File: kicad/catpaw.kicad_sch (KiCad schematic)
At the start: 42 parts, among them J1 Conn_01x01_Socket_red, J2 Conn_01x01_Socket_black, J3 m12,Acode,5pin,femalesocket (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, J4 m8, 4Pin Supply Connector FEM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, J5 m8, 4Pin Supply Connector Bec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, J6 m12,Acode,5pin,femalesocket B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, J7 m12,Acode,5pin,femalesocket C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, J8 Conn_01x01_Pin, SW1 1MD1T1B1M6QES, U1 INA826, U2 LM1458mx

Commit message: Begin Rev1.1
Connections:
- net GND: now also R13.2
- net m8 GNDp: no longer R13.2
- no-connect marks 5 -> 6
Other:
- note added: "(-7.6V)"
- note added: "09/14/26 as per datasheet, (section: ) omit Rg for a gain of 1"
- note added: "09/14/26 simulated via circuitLab omit rakout- connection to input"
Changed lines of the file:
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@@
 		)
 	)
+	(text "09/14/26\nsimulated via circuitLab\nomit rakout- connection to input"
+		(exclude_from_sim no)
+		(at 241.808 125.984 0)
+		(effects
+			(font
+				(size 1.27 1.27)
+			)
+		)
+	)
 	(text "m8 Up+- & m12 Up+- \nare connected in beckhoff"
 		(exclude_from_sim no)
@@
 		)
 	)
+	(text "09/14/26\nas per datasheet, (section:  ) \nomit Rg for a gain of 1"
+		(exclude_from_sim no)
+		(at 86.868 184.15 0)
+		(effects
+			(font
+				(size 1.27 1.27)
+			)
+			(justify left)
+		)
+	)
+	(text "(-7.6V)"
+		(exclude_from_sim no)
+		(at 256.286 116.586 0)
+		(effects
+			(font
+				(size 1.27 1.27)
+			)
+		)
+	)
 	(text "thruhole LED\npanelmount"
 		(exclude_from_sim no)
@@
 	)
 	(no_connect
+		(at 203.2 120.65)
+	)
+	(no_connect
 		(at 63.5 110.49)
 	)
@@
 	(wire
 		(pts
-			(xy 203.2 120.65) (xy 222.25 120.65)
-		)
-		(stroke
-			(width 0)
-			(type default)
-		)
-	)
-	(wire
-		(pts
 			(xy 191.77 149.86) (xy 208.28 149.86)
 		)
@@
 				)
 			)
+		)
+	)
+	(symbol
+		(lib_id "power:GND")
+		(at 222.25 120.65 0)
+		(unit 1)
+		(exclude_from_sim no)
+		(in_bom yes)
+		(on_board yes)
+		(dnp no)
+		(property "Reference" "#PWR06"
+			(at 222.25 127 0)
+			(effects
+				(font
+					(size 1.27 1.27)
+				)
+				(hide yes)
+			)
+		)
+		(property "Value" "GND"
+			(at 222.25 124.714 0)
+			(effects
+				(font
+					(size 1.27 1.27)
+				)
+			)
+		)
+		(property "Footprint" ""
+			(at 222.25 120.65 0)
+			(effects
+				(font
+					(size 1.27 1.27)
+				)
+				(hide yes)
+			)
+		)
+		(property "Datasheet" ""
+			(at 222.25 120.65 0)
+			(effects
+				(font
+					(size 1.27 1.27)
+				)
+				(hide yes)
+			)
+		)
+		(property "Description" "Power symbol creates a global label with name \"GND\" , ground"
+			(at 222.25 120.65 0)
+			(effects
+				(font
+					(size 1.27 1.27)
+				)
+				(hide yes)
+			)
+		)
+		(pin "1"
+		)
+		(instances
+			(project "catpaw"
+				(path "/c6afa226-7a71-49a1-9fd2-6abf112b3631"
+					(reference "#PWR06")
+					(unit 1)
+				)
+			)

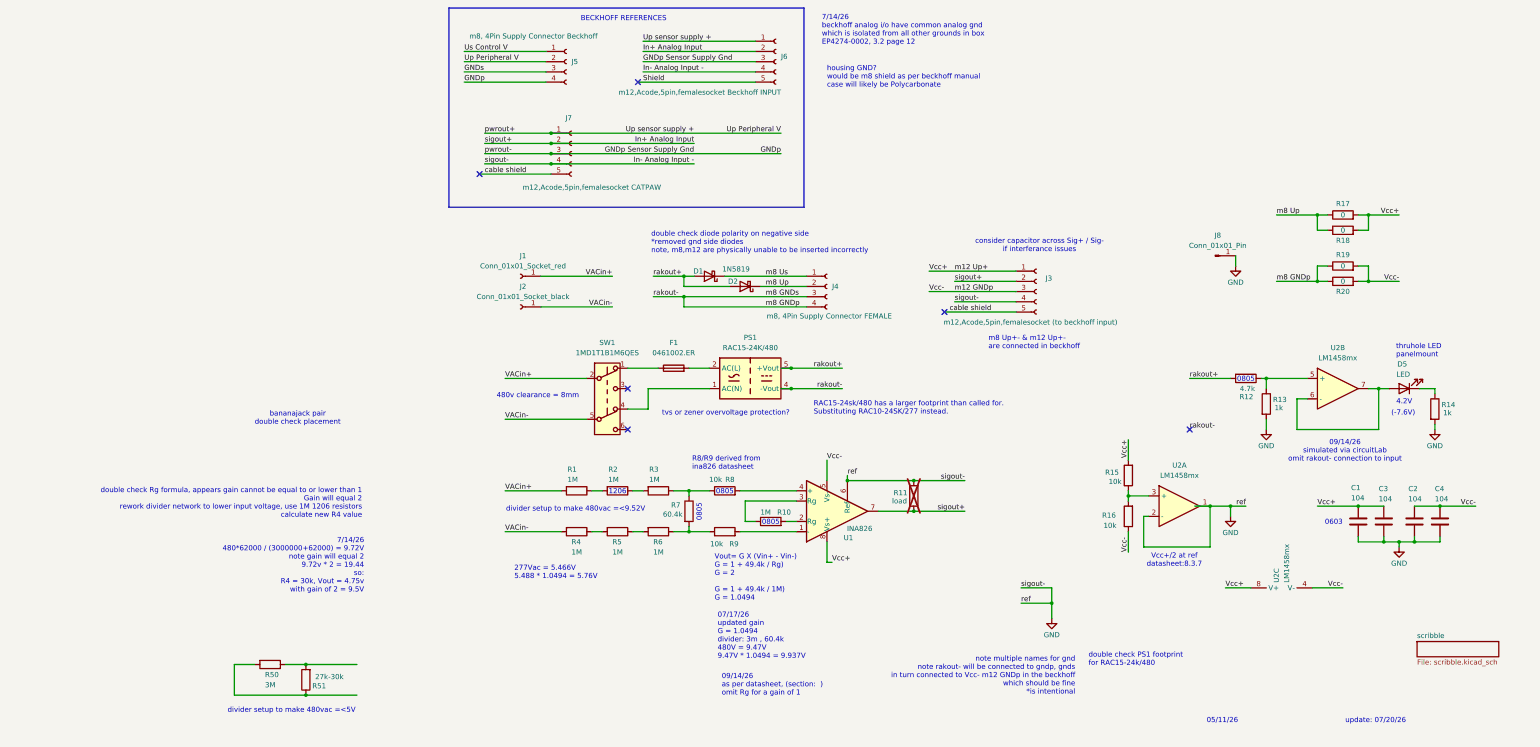
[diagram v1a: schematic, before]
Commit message: added new bode plots
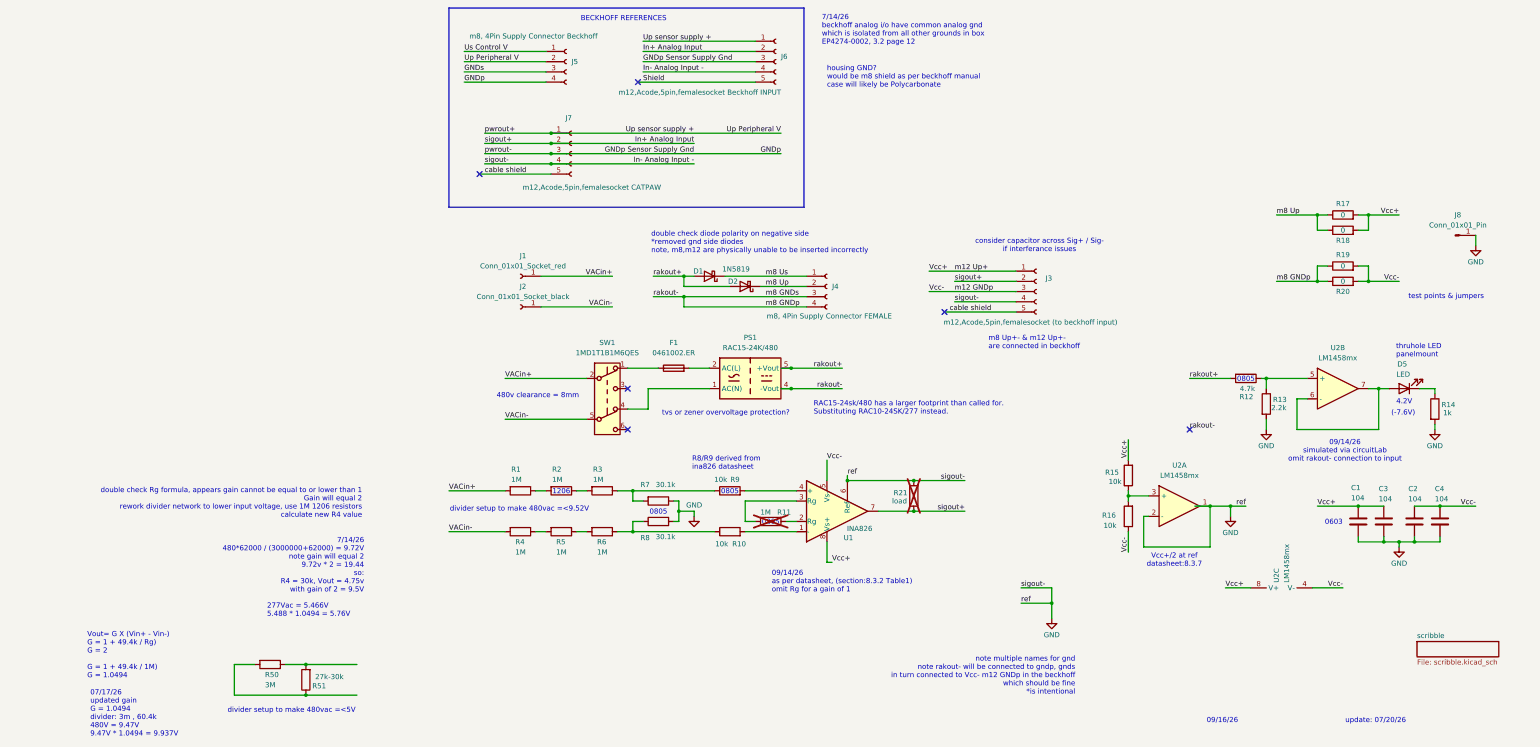
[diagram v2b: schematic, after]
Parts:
- added R8: 30.1k, Resistor_SMD:R_0805_2012Metric_Pad1.20x1.40mm_HandSolder, symbol Device:R
- R11: renamed from R10; now not fitted
- R13: value 1k -> 2.2k
- R18, R19: footprint Resistor_THT:R_Axial_DIN0204_L3.6mm_D1.6mm_P2.54mm_Vertical -> TestPoint:TestPoint_2Pads_Pitch2.54mm_Drill0.8mm
- R7: value 60.4k -> 30.1k
- renumbered R9 to R10, R11 to R21, R8 to R9
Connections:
- net GND: now also R7.1, R8.2
- net at R3.1, R9.1: now also R7.2; no longer R7.1
- net at R10.1, R6.1: now also R8.1; no longer R7.2
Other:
- note added: "09/14/26 as per datasheet, (section:8.3.2 Table1) omit Rg for a gain of 1"
- note added: "09/16/26"
- note added: "test points & jumpers"
- note removed: "05/11/26"
- note removed: "09/14/26 as per datasheet, (section: ) omit Rg for a gain of 1"
- note removed: "bananajack pair double check placement"
- note removed: "double check PS1 footprint for RAC15-24k/480"
- moved on the sheet: J8, R1, R10, R2, R3, R4, R5, R6, R9
